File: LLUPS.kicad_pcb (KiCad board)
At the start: 2 copper layers, 140 x 90 mm, 39 parts, among them J1 USB_C, J2 Output, J3 Debug, Q1 FS8205A, U1 USBLC6-2SC6, U2 BQ24072, U3 HY2113-KB5B, U4 MT3608, U5 AP2112K-3.3, U6 LN61CN3302MR-G

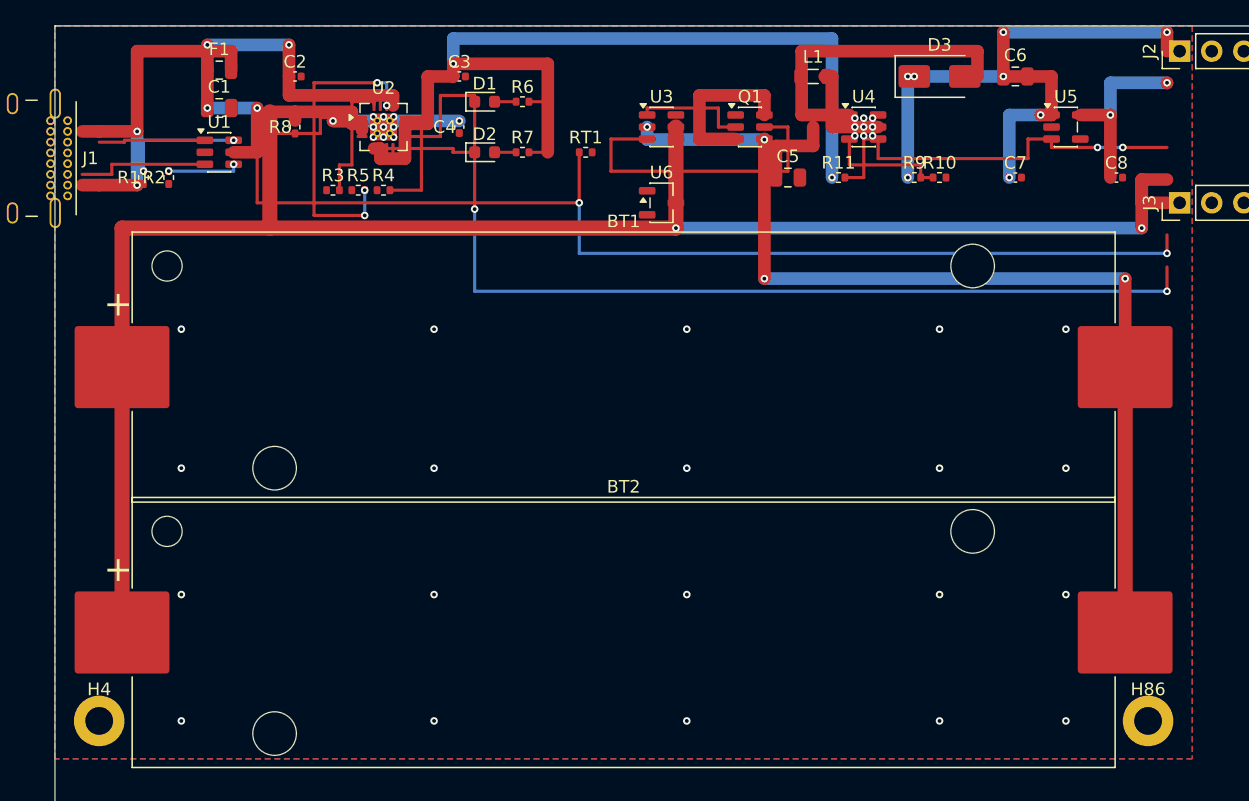
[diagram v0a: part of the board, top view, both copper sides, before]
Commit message: Replace custom A*/RRR router with FreeRouting autorouter
- Created freerouting_runner.py: DSN export → FreeRouting CLI → SES import pipeline
- Subprocess-isolated pcbnew calls to avoid SwigPyObject stale-object bug
- dialog_confirmation_timeout: 0 suppresses blocking FreeRouting dialogs
- clear_traces() removes existing traces before each routing run
- Removed dead code: router.py, conflict.py, grid_builder.py, test_router_grid_behavior.py
- Updated config.py: replaced grid/A*/RRR keys with freerouting_jar/timeout/max_passes
- Updated pipeline.py RoutingEngine to call route_with_freerouting()
- Fixed ExperimentScore.compute() to use passed weights dict
- Updated autoexperiment.py mutations to placement-only params
- Added docs: architecture, scoring, freerouting-plan, footprint-layout
- Cleaned up stale files: LEARNINGS.md, ROUTING_IMPROVEMENTS.md, dashboard.png
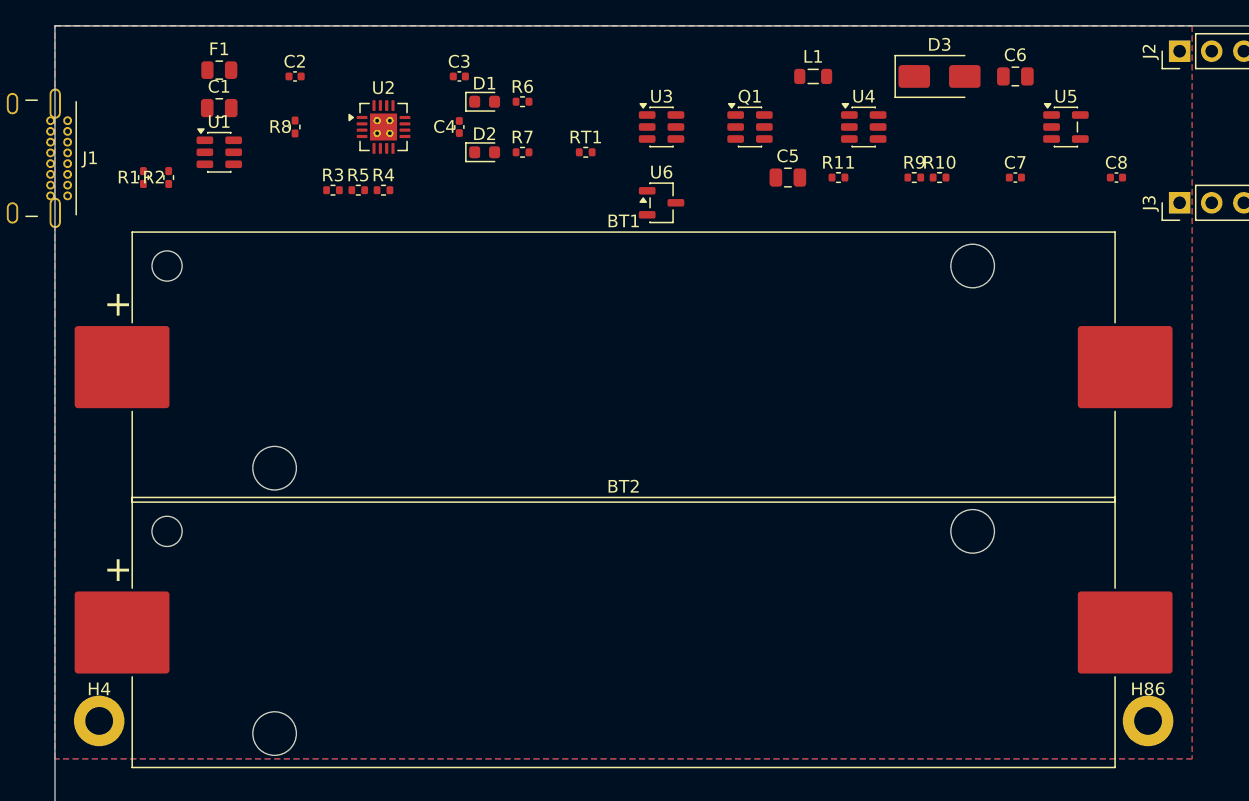
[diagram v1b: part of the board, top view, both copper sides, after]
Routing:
- net /VBAT: track 160.5 -> 0.00 mm, vias 4 -> 0
- net /NTC_SENSE: track 96.5 -> 0.00 mm, vias 2 -> 0
- net /CHG_N: track 81.0 -> 0.00 mm, vias 2 -> 0
- net /CELL_NEG: track 77.9 -> 0.00 mm, vias 4 -> 0
- net /VSYS: track 75.0 -> 0.00 mm, vias 2 -> 0
- net /5V: track 48.7 -> 0.00 mm, vias 8 -> 0
- net /VBUS: track 33.8 -> 0.00 mm, vias 4 -> 0
- net /EN: track 32.3 -> 0.00 mm, vias 2 -> 0
- net Net-(F1-Pad2): track 28.2 -> 0.00 mm, vias 2 -> 0
- net Net-(D3-A): track 25.7 -> 0.00 mm
- net Net-(Q1B-G): track 24.8 -> 0.00 mm
- net Net-(U2-TMR): track 24.1 -> 0.00 mm, vias 4 -> 0
- net /VSYS_BOOST: track 15.2 -> 0.00 mm
- net /3V3: track 14.4 -> 0.00 mm, vias 2 -> 0
- net Net-(Q1A-D): track 13.0 -> 0.00 mm
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
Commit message: Fix battery holder footprint to match BOM
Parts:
- BT1, BT2: footprint Battery:BatteryHolder_Keystone_1042_1x18650 -> LLUPS:BatteryHolder_MYOUNG_BH-18650-A1AJ006

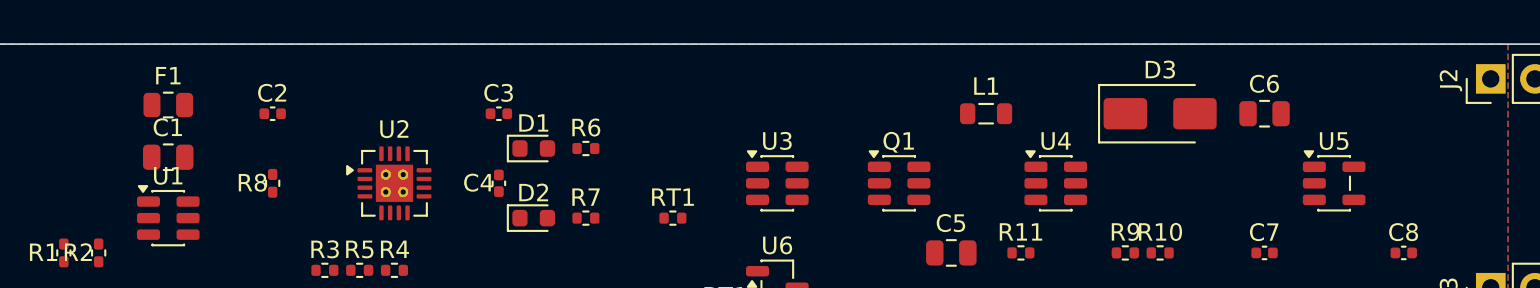
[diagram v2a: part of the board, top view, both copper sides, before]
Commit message: Add generalized KiCad group labeling and schematic splitting
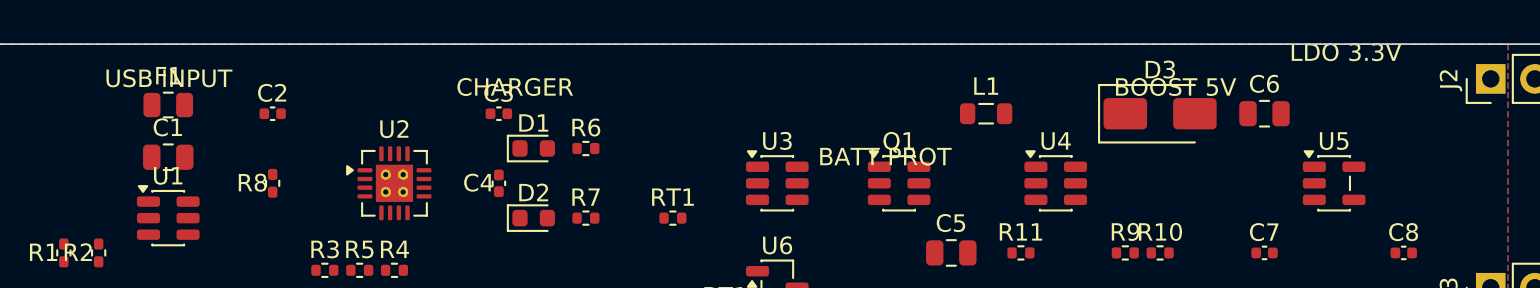
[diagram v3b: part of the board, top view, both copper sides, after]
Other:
- board text added: "BATT PROT"
- board text added: "BOOST 5V"
- board text added: "CHARGER"
- board text added: "LDO 3.3V"
- board text added: "USB INPUT"
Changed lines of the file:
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@@
 	)
 	(embedded_fonts no)
+	(gr_text "USB INPUT"
+		(at 9.33 2.00)
+		(layer "F.SilkS")
+		(uuid "group_label_u1_485f2cce")
+		(effects
+			(font
+				(size 1.0 1.0)
+				(thickness 0.15)
+			)
+			(justify left)
+		)
+	)
+	(gr_text "CHARGER"
+		(at 29.54 2.50)
+		(layer "F.SilkS")
+		(uuid "group_label_u2_7a33ef26")
+		(effects
+			(font
+				(size 1.0 1.0)
+				(thickness 0.15)
+			)
+			(justify left)
+		)
+	)
+	(gr_text "BATT PROT"
+		(at 50.33 6.50)
+		(layer "F.SilkS")
+		(uuid "group_label_u3_2f5f1b7b")
+		(effects
+			(font
+				(size 1.0 1.0)
+				(thickness 0.15)
+			)
+			(justify left)
+		)
+	)
+	(gr_text "BOOST 5V"
+		(at 67.33 2.50)
+		(layer "F.SilkS")
+		(uuid "group_label_u4_c7a6f767")
+		(effects
+			(font
+				(size 1.0 1.0)
+				(thickness 0.15)
+			)
+			(justify left)
+		)
+	)
+	(gr_text "LDO 3.3V"
+		(at 77.43 0.50)
+		(layer "F.SilkS")
+		(uuid "group_label_u5_bcebe28b")
+		(effects
+			(font
+				(size 1.0 1.0)
+				(thickness 0.15)
+			)
+			(justify left)
+		)
+	)
 )
